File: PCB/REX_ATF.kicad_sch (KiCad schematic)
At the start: 9 parts, among them J1 Tandy_100_102_200_option_rom, J2 JTAG, U1 ATF1504ASL-xAx44, U2 29F800BB

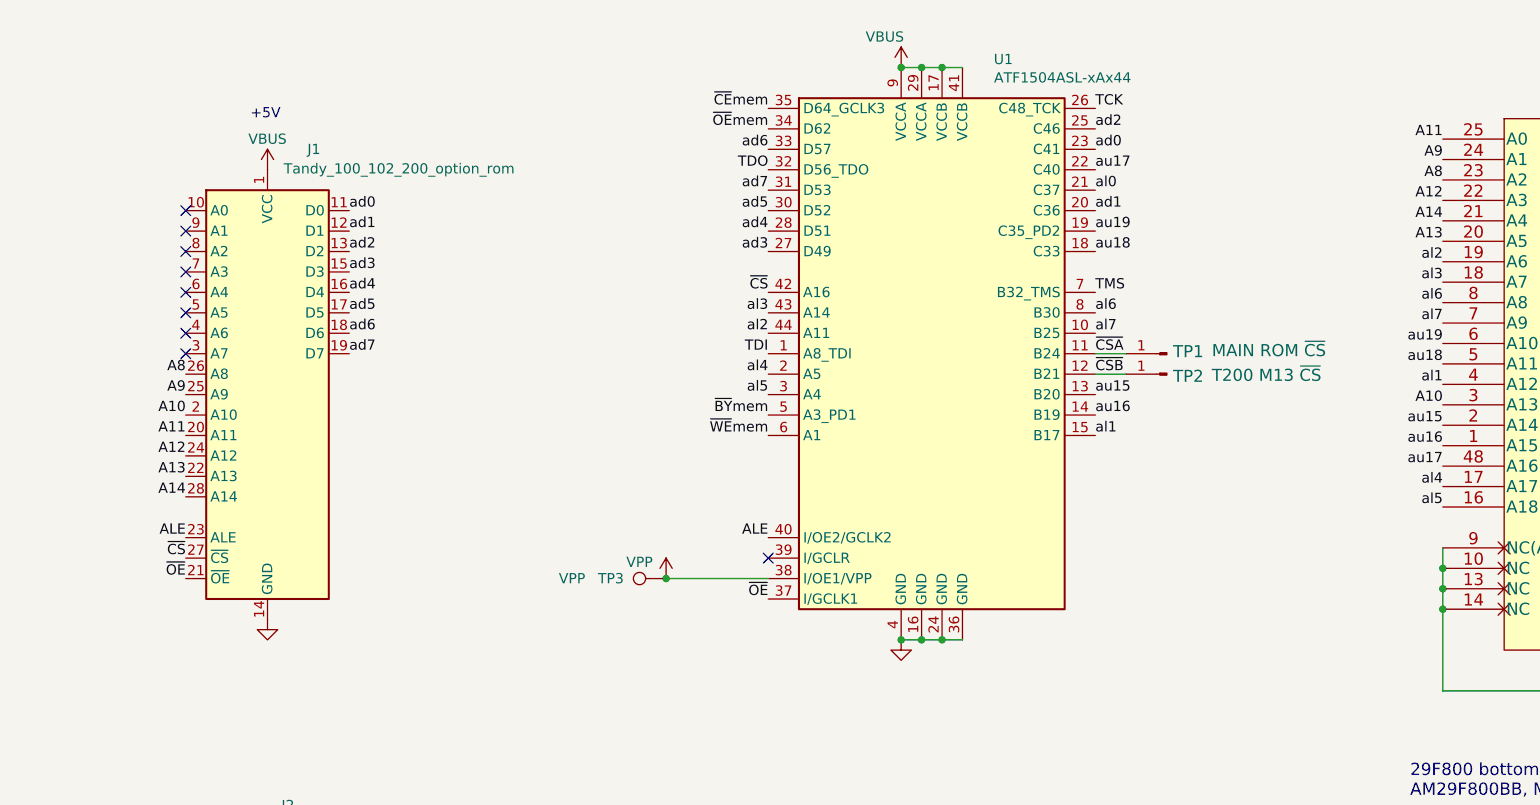
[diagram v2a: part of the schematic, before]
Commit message: external pullups on CSA CSB
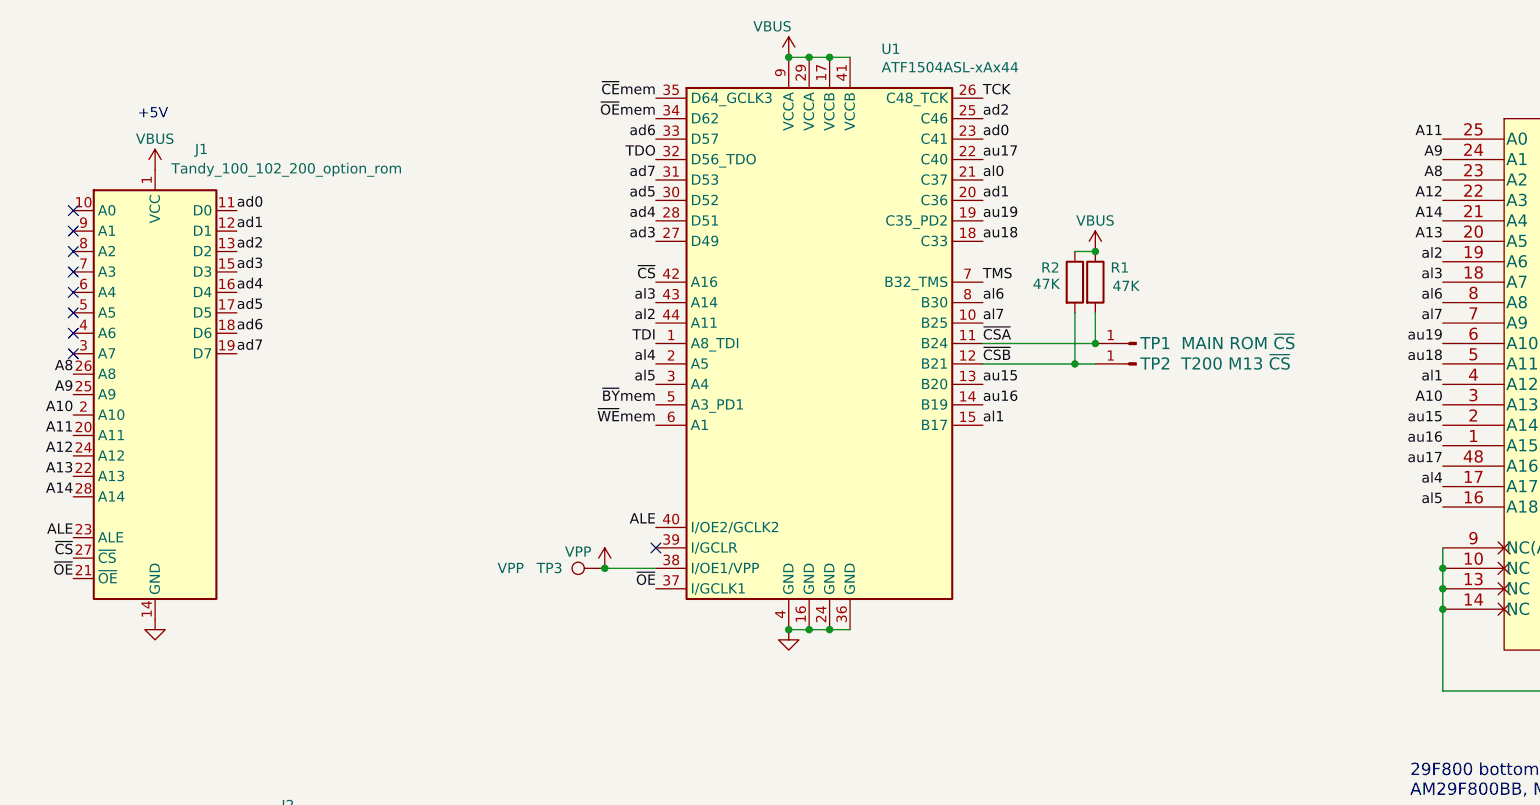
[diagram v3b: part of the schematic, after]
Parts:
- added R1, R2: 47K, 000_LOCAL:R_0805, symbol 000_LOCAL:R
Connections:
- net VBUS: now also R1.1, R2.1
- net ~{CSA}: now also R1.2
- net ~{CSB}: now also R2.2
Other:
- moved on the sheet: J1, TP1, TP2, TP3, U1

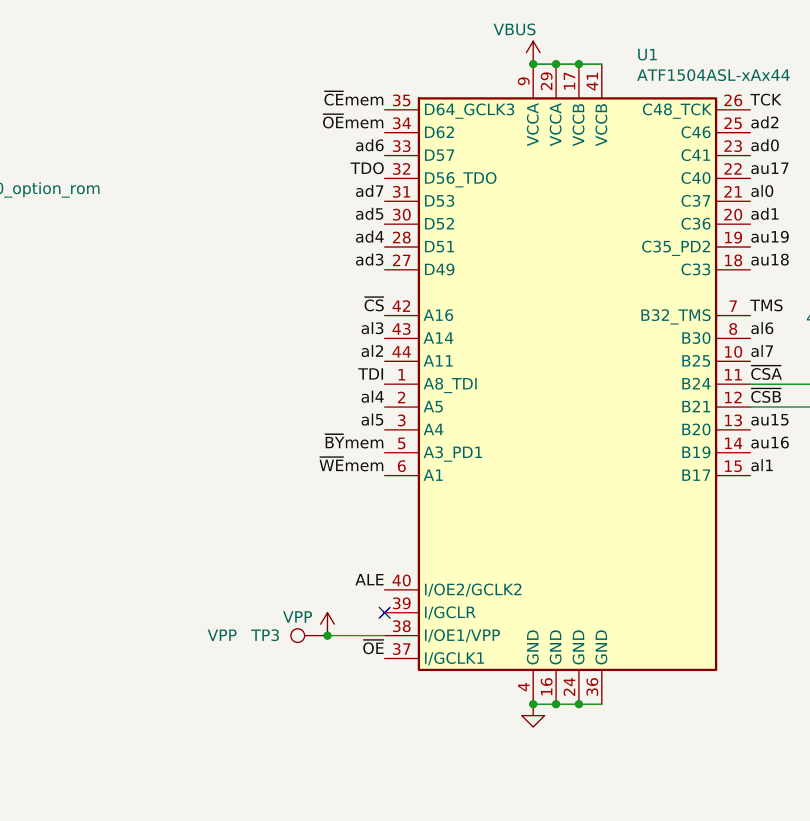
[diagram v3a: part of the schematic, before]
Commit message: enable pin keeper option
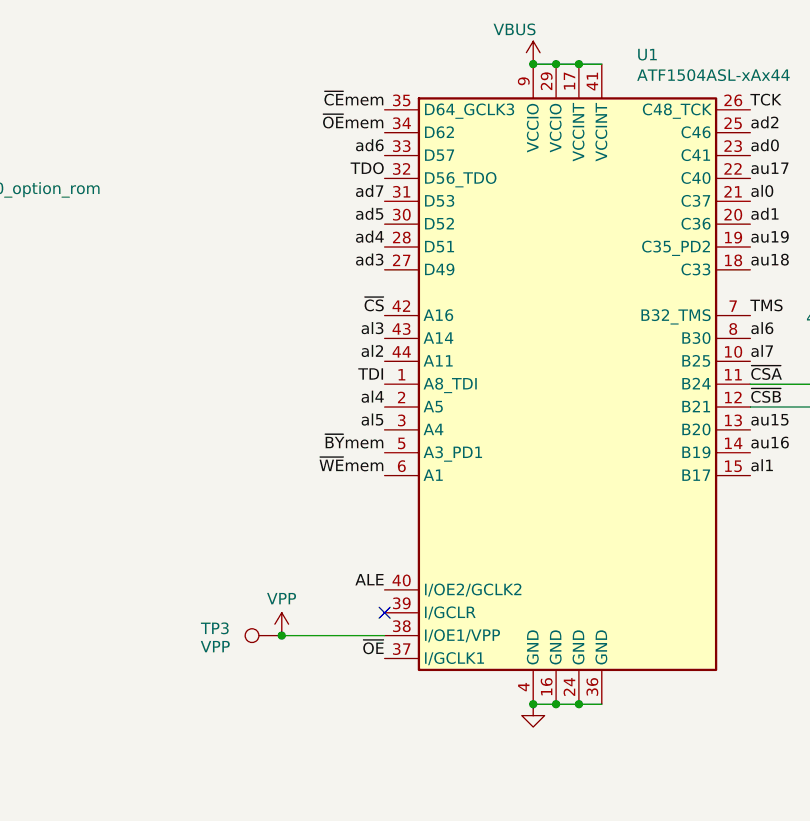
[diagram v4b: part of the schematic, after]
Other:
- moved on the sheet: TP3
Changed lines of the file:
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@@
 	)
 	(junction
-		(at 106.68 104.14)
+		(at 101.6 104.14)
 		(diameter 0)
 		(color 0 0 0 0)
@@
 	(wire
 		(pts
-			(xy 106.68 104.14) (xy 113.03 104.14)
+			(xy 246.38 83.82) (xy 246.38 86.36)
 		)
 		(stroke
@@
 	(wire
 		(pts
-			(xy 246.38 83.82) (xy 246.38 86.36)
+			(xy 210.82 101.6) (xy 210.82 104.14)
 		)
 		(stroke
@@
 	(wire
 		(pts
-			(xy 210.82 101.6) (xy 210.82 104.14)
+			(xy 167.64 72.39) (xy 167.64 76.2)
 		)
 		(stroke
@@
 	(wire
 		(pts
-			(xy 167.64 72.39) (xy 167.64 76.2)
+			(xy 101.6 104.14) (xy 113.03 104.14)
 		)
 		(stroke
@@
 	(symbol
 		(lib_id "000_LOCAL:TestPoint")
-		(at 106.68 104.14 90)
+		(at 101.6 104.14 90)
 		(unit 1)
 		(exclude_from_sim no)
@@
 		(dnp no)
 		(property "Reference" "TP3"
-			(at 99.822 104.14 90)
+			(at 94.234 103.378 90)
 			(effects
 				(font
@@
 		)
 		(property "Value" "VPP"
-			(at 94.996 104.14 90)
+			(at 101.6 100.076 90)
 			(effects
 				(font
@@
 		)
 		(property "Footprint" "000_LOCAL:TP_D0.8"
-			(at 106.68 99.06 0)
+			(at 101.6 99.06 0)
 			(effects
 				(font
@@
 		)
 		(property "Datasheet" "~"
-			(at 106.68 99.06 0)
+			(at 101.6 99.06 0)
 			(effects
 				(font
@@
 		)
 		(property "Description" "test point"
-			(at 106.68 104.14 0)
+			(at 101.6 104.14 0)
 			(effects
 				(font
@@
 	(symbol
 		(lib_id "power:VPP")
-		(at 106.68 104.14 0)
+		(at 101.6 104.14 0)
 		(unit 1)
 		(exclude_from_sim no)
@@
 		(dnp no)
 		(property "Reference" "#PWR08"
-			(at 106.68 107.95 0)
+			(at 101.6 107.95 0)
 			(effects
 				(font
@@
 		)
 		(property "Value" "VPP"
-			(at 103.378 102.108 0)
+			(at 94.234 105.41 0)
 			(effects
 				(font
@@
 		)
 		(property "Footprint" ""
-			(at 106.68 104.14 0)
+			(at 101.6 104.14 0)
 			(effects
 				(font
@@
 		)
 		(property "Datasheet" ""
-			(at 106.68 104.14 0)
+			(at 101.6 104.14 0)
 			(effects
 				(font
@@
 		)
 		(property "Description" "Power symbol creates a global label with name \"VPP\""
-			(at 106.68 104.14 0)
-			(effects
-				(font
+			(at 101.6 104.14 0)
+			(effects
+				(font

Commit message: minor pcb touches, update readme
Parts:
- added N1: Housing, 000_LOCAL:Housing_Molex78802_PCB_28, symbol 000_LOCAL:Housing
- C1, C2: MPN (none) -> CL21B105KAFNNNE
- J1: value Tandy_100_102_200_option_rom -> Tandy_100_102_200_option_rom socket edge connections; now left out of the parts list
- J2, TP3: now left out of the parts list
- R1, R2: MPN (none) -> RC0805JR-0747KL
- TP1: value MAIN ROM ~{CS} -> MAIN_ROM_~{CS}; now left out of the parts list
- TP2: value T200 M13 ~{CS} -> T200_M13_~{CS}; now left out of the parts list
- U1: MPN (none) -> ATF1504ASL-25AU44
- U2: MPN (none) -> M29F800FB5AN6F2
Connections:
- net ~{BY}mem: now also U1.42 (A16); no longer U1.5 (A3_PD1)
- net ~{CS}: now also U1.5 (A3_PD1); no longer U1.42 (A16)
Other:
- note added: "29F800 bottom-boot TSOP-48 AM29F800BB, MX29F800CB (MX29F800CBTI-70G), M29F800FB (M29F800FB5AN6F2)"
- note removed: "29F800 bottom-boot TSOP-48 AM29F800BB, MX29F800CB, M29F800FB"
- moved on the sheet: C1, R2, TP1, TP2, TP3, U1
